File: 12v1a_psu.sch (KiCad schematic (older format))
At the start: 18 parts, among them J1 AC_in, J2 P1, J3 P2, J4 Vout, Q1 BD440, SW1 SW_SPST, U1 LM7812

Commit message: Work on pcb layout
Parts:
- J1, J2, J3, SW1: footprint Connector_Wire:SolderWirePad_1x02_P7.62mm_Drill2.5mm -> Connector_Wire:SolderWirePad_1x02_P5.08mm_Drill1.5mm
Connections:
- wire segments 65 -> 69
- no-connect marks 4 -> 0
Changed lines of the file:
@@
 F 0 "SW1" H 2150 3235 50  0000 C CNN
 F 1 "SW_SPST" H 2150 3144 50  0000 C CNN
-F 2 "Connector_Wire:SolderWirePad_1x02_P7.62mm_Drill2.5mm" H 2150 3000 50  0001 C CNN
+F 2 "Connector_Wire:SolderWirePad_1x02_P5.08mm_Drill1.5mm" H 2150 3000 50  0001 C CNN
 F 3 "~" H 2150 3000 50  0001 C CNN
 	1    2150 3000
@@
 Wire Wire Line
 	2450 3000 2450 2750
-NoConn ~ 3500 2950
-NoConn ~ 3500 3050
 Wire Wire Line
 	6000 3000 6650 3000
@@
 F 0 "J1" H 1518 2775 50  0000 C CNN
 F 1 "AC_in" H 1518 2866 50  0000 C CNN
-F 2 "Connector_Wire:SolderWirePad_1x02_P7.62mm_Drill2.5mm" H 1600 3100 50  0001 C CNN
+F 2 "Connector_Wire:SolderWirePad_1x02_P5.08mm_Drill1.5mm" H 1600 3100 50  0001 C CNN
 F 3 "~" H 1600 3100 50  0001 C CNN
 	1    1600 3100
@@
 F 0 "J2" V 2814 2262 50  0000 R CNN
 F 1 "P1" V 2723 2262 50  0000 R CNN
-F 2 "Connector_Wire:SolderWirePad_1x02_P7.62mm_Drill2.5mm" H 2850 2450 50  0001 C CNN
+F 2 "Connector_Wire:SolderWirePad_1x02_P5.08mm_Drill1.5mm" H 2850 2450 50  0001 C CNN
 F 3 "~" H 2850 2450 50  0001 C CNN
 	1    2850 2450
@@
 F 0 "J3" V 2822 3630 50  0000 L CNN
 F 1 "P2" V 2913 3630 50  0000 L CNN
-F 2 "Connector_Wire:SolderWirePad_1x02_P7.62mm_Drill2.5mm" H 2950 3550 50  0001 C CNN
+F 2 "Connector_Wire:SolderWirePad_1x02_P5.08mm_Drill1.5mm" H 2950 3550 50  0001 C CNN
 F 3 "~" H 2950 3550 50  0001 C CNN
 	1    2950 3550
 	0    1    1    0
 $EndComp
-NoConn ~ 2950 2650
 Wire Wire Line
 	2450 2750 2850 2750
@@
 	2850 2650 2850 2750
 Connection ~ 2850 2750
-NoConn ~ 2950 3350
 Wire Wire Line
 	2850 3350 2850 3250
@@
 Wire Wire Line
 	2450 3250 2850 3250
+Wire Wire Line
+	2950 3350 2950 3050
+Wire Wire Line
+	2950 3050 3500 3050
+Wire Wire Line
+	2950 2950 2950 2650
+Wire Wire Line
+	3500 2950 2950 2950
 $EndSCHEMATC

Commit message: Add filter caps, misc changes
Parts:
- removed J1: AC_in, Connector_Wire:SolderWirePad_1x02_P5.08mm_Drill1.5mm, symbol Connector_Generic:Conn_01x02
- removed Q1: BD440, Package_TO_SOT_THT:TO-126-3_Vertical, symbol Transistor_BJT:BD440
- removed SW1: SW_SPST, Connector_Wire:SolderWirePad_1x02_P5.08mm_Drill1.5mm, symbol Switch:SW_SPST
- removed U1: LM7812, Package_TO_SOT_THT:TO-220-3_Vertical, symbol Regulator_Linear:LM7812_TO220
- added C?: 1uF, symbol Device:C
- added C?: 2200u, Capacitor_THT:CP_Radial_D30.0mm_P10.00mm_SnapIn, symbol Device:CP
- added J?: AC_IN, symbol Connector_Generic:Conn_01x03
- added Q?: Q_PNP_BCE, symbol Device:Q_PNP_BCE
- added U1: L7812, Package_TO_SOT_THT:TO-220-3_Vertical, symbol Regulator_Linear:L7812
- C1: value 10000u -> 2200u
- R2: Field4 (none) -> 1/2W
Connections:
- net labels added: AC_E, AC_L, AC_N
- wire segments 69 -> 75
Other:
- note added: "TODO: use L01-6363 instead"
- moved on the sheet: C1, C2, C3, D5, J2, J3, J4, R1, TR1

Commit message: Clean up symbol/footprint libs, add cad models
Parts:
- removed J?: AC_IN, symbol Connector_Generic:Conn_01x03
- added H1, H2, H3, H4: PTH_M3, MountingHole:MountingHole_3.2mm_M3_Pad_Via, symbol Mechanical:MountingHole_Pad
- added J1: AC_IN, Connector_Wire:SolderWirePad_1x02_P5.08mm_Drill1.5mm, symbol Connector_Generic:Conn_01x02
- C1: footprint Capacitor_THT:CP_Radial_D30.0mm_P10.00mm_SnapIn -> (none)
- C2: renamed from C?; footprint Capacitor_THT:CP_Radial_D30.0mm_P10.00mm_SnapIn -> (none)
- C3: renamed from C?; footprint (none) -> Capacitor_THT:C_Rect_L18.0mm_W8.0mm_P15.00mm_FKS3_FKP3
- C4: renamed from C2; footprint Capacitor_THT:C_Disc_D5.0mm_W2.5mm_P2.50mm -> (none)
- C5: renamed from C3; footprint Capacitor_THT:C_Disc_D3.8mm_W2.6mm_P2.50mm -> (none)
- J4: footprint Connector_BarrelJack:BarrelJack_Horizontal -> 12v1a_psu:BarrelJack_Horizontal
- TR1: footprint L01-6353:Transformer_L01-6353 -> 12v1a_psu:L01-6363
- gave numbers to parts that had none: 1
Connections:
- net AC_L: now also J1.2 (Pin_2)
- net AC_N: now also J1.1 (Pin_1)
- net GND: now also H1.1, H2.1, H3.1, H4.1
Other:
- note removed: "TODO: use L01-6363 instead"
- moved on the sheet: C1, C2, C3, C4, C5, D1, D2, D3, D4, D5, J2, J3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

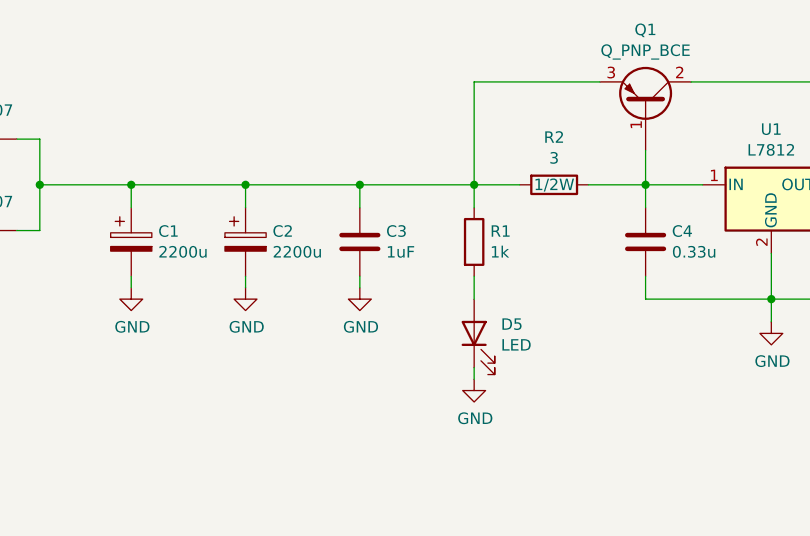
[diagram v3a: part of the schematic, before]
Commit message: Fix cap value
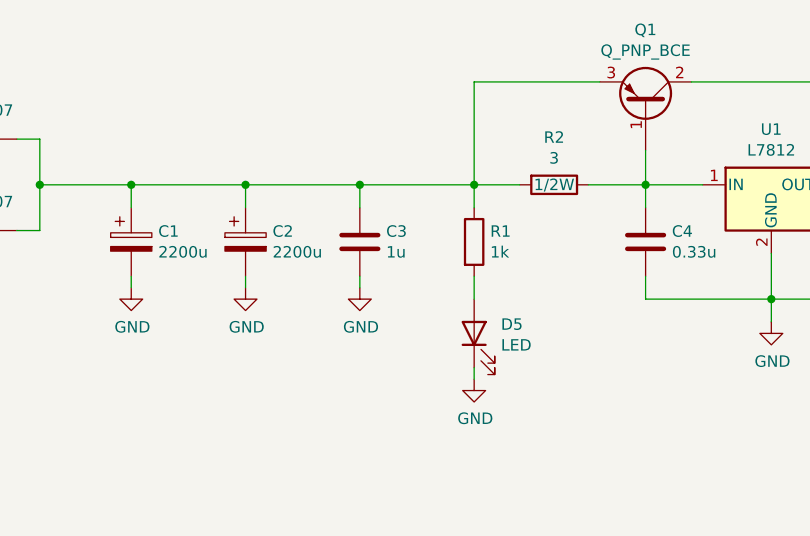
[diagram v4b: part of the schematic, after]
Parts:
- C3: value 1uF -> 1u
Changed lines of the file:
@@
 P 5850 3250
 F 0 "C3" H 5965 3296 50  0000 L CNN
-F 1 "1uF" H 5965 3205 50  0000 L CNN
+F 1 "1u" H 5965 3205 50  0000 L CNN
 F 2 "Capacitor_THT:C_Rect_L18.0mm_W8.0mm_P15.00mm_FKS3_FKP3" H 5888 3100 50  0001 C CNN
 F 3 "~" H 5850 3250 50  0001 C CNN

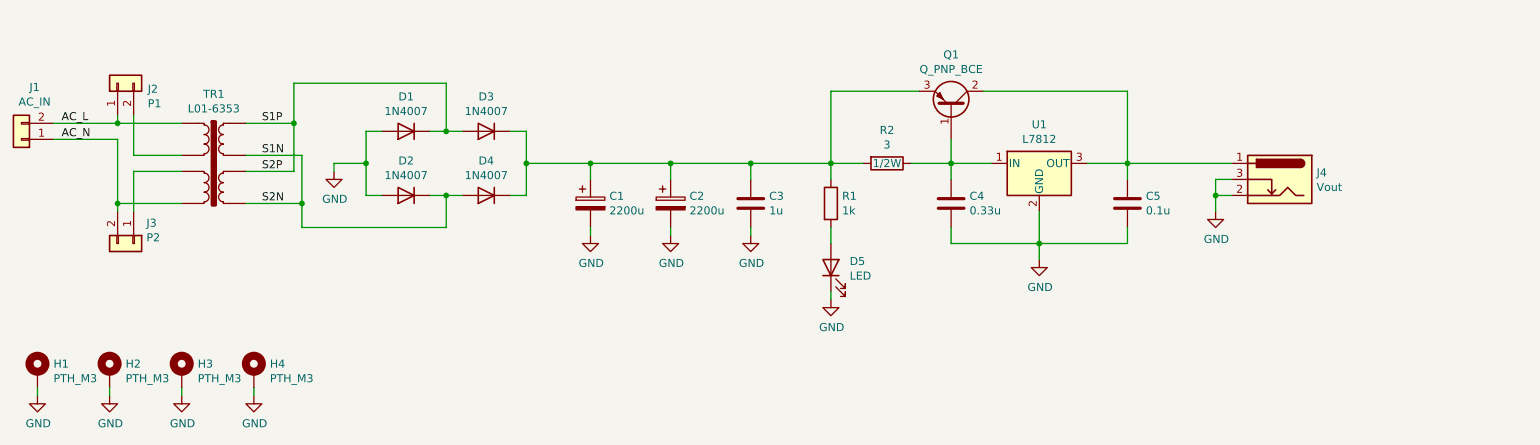
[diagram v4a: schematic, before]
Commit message: Chose bjt for reg, picked footprints
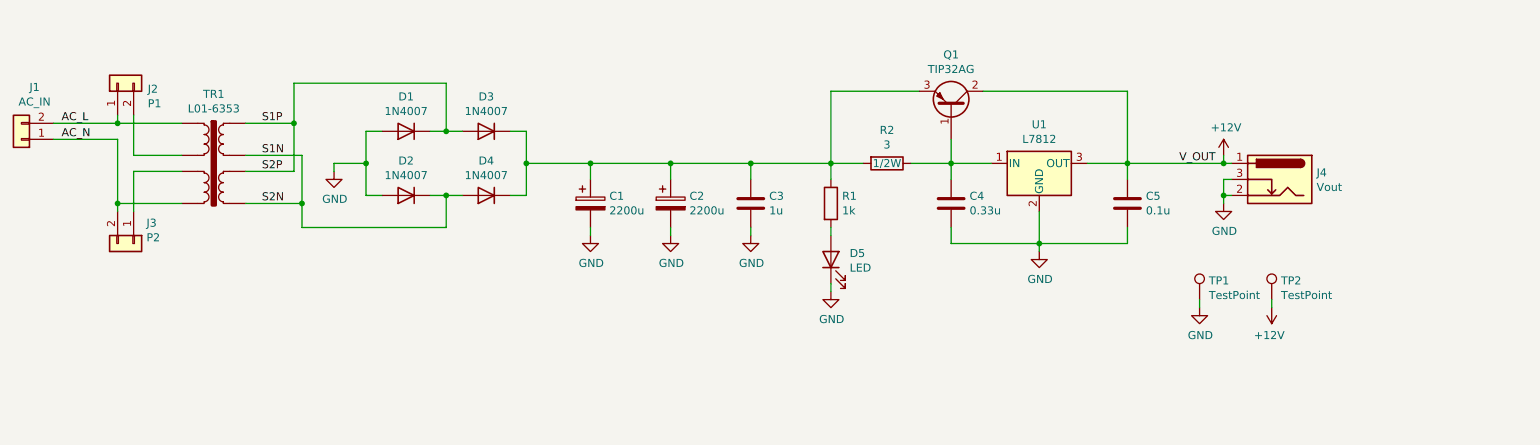
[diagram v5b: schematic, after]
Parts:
- removed H1, H2, H3, H4: PTH_M3, MountingHole:MountingHole_3.2mm_M3_Pad_Via, symbol Mechanical:MountingHole_Pad
- added TP1: TestPoint, TestPoint:TestPoint_THTPad_2.0x2.0mm_Drill1.0mm, symbol Connector:TestPoint
- added TP2: TestPoint, TestPoint:TestPoint_THTPad_D2.0mm_Drill1.0mm, symbol Connector:TestPoint
- C1, C2: footprint (none) -> Capacitor_THT:CP_Radial_D16.0mm_P7.50mm
- C4: footprint (none) -> Capacitor_THT:C_Rect_L7.2mm_W3.5mm_P5.00mm_FKS2_FKP2_MKS2_MKP2
- C5: footprint (none) -> Capacitor_THT:C_Rect_L7.2mm_W2.5mm_P5.00mm_FKS2_FKP2_MKS2_MKP2
- J1, J2, J3: footprint Connector_Wire:SolderWirePad_1x02_P5.08mm_Drill1.5mm -> Connector_Wire:SolderWire-0.75sqmm_1x02_P4.8mm_D1.25mm_OD2.3mm
- Q1: value Q_PNP_BCE -> TIP32AG; footprint (none) -> Package_TO_SOT_THT:TO-220-3_Vertical
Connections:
- net GND: now also TP1.1
- net +12V: now reaches C5.1, J4.1, Q1.2 (C), U1.3 (OUT)
- net +12V: now also TP2.1
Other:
- moved on the sheet: D5
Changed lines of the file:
@@
 F 0 "C1" H 4968 3296 50  0000 L CNN
 F 1 "2200u" H 4968 3205 50  0000 L CNN
-F 2 "" H 4888 3100 50  0001 C CNN
+F 2 "Capacitor_THT:CP_Radial_D16.0mm_P7.50mm" H 4888 3100 50  0001 C CNN
 F 3 "~" H 4850 3250 50  0001 C CNN
 	1    4850 3250
@@
 L Device:LED D5
 U 1 1 5CCC0EA2
-P 6350 3650
-F 0 "D5" V 6389 3533 50  0000 R CNN
-F 1 "LED" V 6298 3533 50  0000 R CNN
-F 2 "LED_THT:LED_D5.0mm_Horizontal_O1.27mm_Z3.0mm" H 6350 3650 50  0001 C CNN
-F 3 "~" H 6350 3650 50  0001 C CNN
-	1    6350 3650
+P 6350 3600
+F 0 "D5" V 6389 3483 50  0000 R CNN
+F 1 "LED" V 6298 3483 50  0000 R CNN
+F 2 "LED_THT:LED_D5.0mm_Horizontal_O1.27mm_Z3.0mm" H 6350 3600 50  0001 C CNN
+F 3 "~" H 6350 3600 50  0001 C CNN
+	1    6350 3600
 	0    -1   -1   0
 $EndComp
 Wire Wire Line
-	6350 3500 6350 3400
+	6350 3450 6350 3400
 $Comp
 L Device:R R1
@@
 $EndComp
 Wire Wire Line
-	6350 3850 6350 3800
+	6350 3800 6350 3750
 $Comp
 L power:GND #PWR09
 U 1 1 5CCC34E6
-P 6350 3850
-F 0 "#PWR09" H 6350 3600 50  0001 C CNN
-F 1 "GND" H 6355 3677 50  0000 C CNN
-F 2 "" H 6350 3850 50  0001 C CNN
-F 3 "" H 6350 3850 50  0001 C CNN
-	1    6350 3850
+P 6350 3800
+F 0 "#PWR09" H 6350 3550 50  0001 C CNN
+F 1 "GND" H 6355 3627 50  0000 C CNN
+F 2 "" H 6350 3800 50  0001 C CNN
+F 3 "" H 6350 3800 50  0001 C CNN
+	1    6350 3800
 	1    0    0    -1
 $EndComp
@@
 P 7100 2650
 F 0 "Q1" V 7428 2650 50  0000 C CNN
-F 1 "Q_PNP_BCE" V 7337 2650 50  0000 C CNN
-F 2 "" H 7300 2750 50  0001 C CNN
+F 1 "TIP32AG" V 7337 2650 50  0000 C CNN
+F 2 "Package_TO_SOT_THT:TO-220-3_Vertical" H 7300 2750 50  0001 C CNN
 F 3 "~" H 7100 2650 50  0001 C CNN
 	1    7100 2650
@@
 $EndComp
 Wire Wire Line
-	8200 3000 8850 3000
-Wire Wire Line
-	8750 3200 8750 3300
-Connection ~ 8750 3200
-Wire Wire Line
-	8850 3200 8750 3200
-Wire Wire Line
-	8750 3100 8750 3200
-Wire Wire Line
-	8850 3100 8750 3100
-Wire Wire Line
 	6350 2550 6900 2550
 Wire Wire Line
@@
 L power:GND #PWR011
 U 1 1 5CCF183A
-P 8750 3300
-F 0 "#PWR011" H 8750 3050 50  0001 C CNN
-F 1 "GND" H 8755 3127 50  0000 C CNN
-F 2 "" H 8750 3300 50  0001 C CNN
-F 3 "" H 8750 3300 50  0001 C CNN
-	1    8750 3300
+P 8800 3250
+F 0 "#PWR011" H 8800 3000 50  0001 C CNN
+F 1 "GND" H 8805 3077 50  0000 C CNN
+F 2 "" H 8800 3250 50  0001 C CNN
+F 3 "" H 8800 3250 50  0001 C CNN
+	1    8800 3250
 	1    0    0    -1
 $EndComp
@@
 Connection ~ 7650 3500
 Wire Wire Line
-	7650 3500 7650 3600
+	7650 3500 7650 3550
 Wire Wire Line
 	8200 3500 8200 3400
@@
 L power:GND #PWR010
 U 1 1 5CC06751
-P 7650 3600
-F 0 "#PWR010" H 7650 3350 50  0001 C CNN
-F 1 "GND" H 7655 3427 50  0000 C CNN
-F 2 "" H 7650 3600 50  0001 C CNN
-F 3 "" H 7650 3600 50  0001 C CNN
-	1    7650 3600
+P 7650 3550
+F 0 "#PWR010" H 7650 3300 50  0001 C CNN
+F 1 "GND" H 7655 3377 50  0000 C CNN
+F 2 "" H 7650 3550 50  0001 C CNN
+F 3 "" H 7650 3550 50  0001 C CNN
+	1    7650 3550
 	1    0    0    -1
 $EndComp
@@
 F 0 "C4" H 7215 3296 50  0000 L CNN
 F 1 "0.33u" H 7215 3205 50  0000 L CNN
-F 2 "" H 7138 3100 50  0001 C CNN
+F 2 "Capacitor_THT:C_Rect_L7.2mm_W3.5mm_P5.00mm_FKS2_FKP2_MKS2_MKP2" H 7138 3100 50  0001 C CNN
 F 3 "~" H 7100 3250 50  0001 C CNN
 	1    7100 3250
@@
 F 0 "C5" H 8315 3296 50  0000 L CNN
 F 1 "0.1u" H 8315 3205 50  0000 L CNN
-F 2 "" H 8238 3100 50  0001 C CNN
+F 2 "Capacitor_THT:C_Rect_L7.2mm_W2.5mm_P5.00mm_FKS2_FKP2_MKS2_MKP2" H 8238 3100 50  0001 C CNN
 F 3 "~" H 8200 3250 50  0001 C CNN
 	1    8200 3250
@@
 F 0 "C2" H 5468 3296 50  0000 L CNN
 F 1 "2200u" H 5468 3205 50  0000 L CNN
-F 2 "" H 5388 3100 50  0001 C CNN
+F 2 "Capacitor_THT:CP_Radial_D16.0mm_P7.50mm" H 5388 3100 50  0001 C CNN
 F 3 "~" H 5350 3250 50  0001 C CNN
 	1    5350 3250
@@
 Wire Wire Line
 	5350 3000 5850 3000
-$Comp
-L Mechanical:MountingHole_Pad H1
-U 1 1 5FB1F325
-P 1400 4300
-F 0 "H1" H 1500 4349 50  0000 L CNN
-F 1 "PTH_M3" H 1500 4258 50  0000 L CNN
-F 2 "MountingHole:MountingHole_3.2mm_M3_Pad_Via" H 1400 4300 50  0001 C CNN
-F 3 "~" H 1400 4300 50  0001 C CNN
-	1    1400 4300
-	1    0    0    -1
-$EndComp
-$Comp
-L power:GND #PWR01
-U 1 1 5FB21FB5
-P 1400 4450
-F 0 "#PWR01" H 1400 4200 50  0001 C CNN
-F 1 "GND" H 1405 4277 50  0000 C CNN
-F 2 "" H 1400 4450 50  0001 C CNN
-F 3 "" H 1400 4450 50  0001 C CNN
-	1    1400 4450
-	1    0    0    -1
-$EndComp
-Wire Wire Line
-	1400 4450 1400 4400
-$Comp
-L Mechanical:MountingHole_Pad H2
-U 1 1 5FB2637E
-P 1850 4300
-F 0 "H2" H 1950 4349 50  0000 L CNN
-F 1 "PTH_M3" H 1950 4258 50  0000 L CNN
-F 2 "MountingHole:MountingHole_3.2mm_M3_Pad_Via" H 1850 4300 50  0001 C CNN
-F 3 "~" H 1850 4300 50  0001 C CNN
-	1    1850 4300
-	1    0    0    -1
-$EndComp
-$Comp
-L power:GND #PWR02
-U 1 1 5FB26384
-P 1850 4450
-F 0 "#PWR02" H 1850 4200 50  0001 C CNN
-F 1 "GND" H 1855 4277 50  0000 C CNN
-F 2 "" H 1850 4450 50  0001 C CNN
-F 3 "" H 1850 4450 50  0001 C CNN
-	1    1850 4450
-	1    0    0    -1
-$EndComp
-Wire Wire Line
-	1850 4450 1850 4400
-$Comp
-L Mechanical:MountingHole_Pad H3
-U 1 1 5FB27F25
-P 2300 4300
-F 0 "H3" H 2400 4349 50  0000 L CNN
-F 1 "PTH_M3" H 2400 4258 50  0000 L CNN
-F 2 "MountingHole:MountingHole_3.2mm_M3_Pad_Via" H 2300 4300 50  0001 C CNN
-F 3 "~" H 2300 4300 50  0001 C CNN
-	1    2300 4300
-	1    0    0    -1
-$EndComp
-$Comp
-L power:GND #PWR03
-U 1 1 5FB27F2B
-P 2300 4450
-F 0 "#PWR03" H 2300 4200 50  0001 C CNN
-F 1 "GND" H 2305 4277 50  0000 C CNN
-F 2 "" H 2300 4450 50  0001 C CNN
-F 3 "" H 2300 4450 50  0001 C CNN
-	1    2300 4450
-	1    0    0    -1
-$EndComp
-Wire Wire Line
-	2300 4450 2300 4400
-$Comp
-L Mechanical:MountingHole_Pad H4
-U 1 1 5FB29C79
-P 2750 4300
-F 0 "H4" H 2850 4349 50  0000 L CNN
-F 1 "PTH_M3" H 2850 4258 50  0000 L CNN
-F 2 "MountingHole:MountingHole_3.2mm_M3_Pad_Via" H 2750 4300 50  0001 C CNN
-F 3 "~" H 2750 4300 50  0001 C CNN
-	1    2750 4300
-	1    0    0    -1
-$EndComp
-$Comp
-L power:GND #PWR04
-U 1 1 5FB29C7F
-P 2750 4450
-F 0 "#PWR04" H 2750 4200 50  0001 C CNN
-F 1 "GND" H 2755 4277 50  0000 C CNN
-F 2 "" H 2750 4450 50  0001 C CNN
-F 3 "" H 2750 4450 50  0001 C CNN
-	1    2750 4450
-	1    0    0    -1
-$EndComp
-Wire Wire Line
-	2750 4450 2750 4400
 Wire Wire Line
 	1900 2850 1900 3250
@@
 F 0 "J3" V 1872 3580 50  0000 L CNN
 F 1 "P2" V 1963 3580 50  0000 L CNN
-F 2 "Connector_Wire:SolderWirePad_1x02_P5.08mm_Drill1.5mm" H 2000 3500 50  0001 C CNN
+F 2 "Connector_Wire:SolderWire-0.75sqmm_1x02_P4.8mm_D1.25mm_OD2.3mm" H 2000 3500 50  0001 C CNN
 F 3 "~" H 2000 3500 50  0001 C CNN
 	1    2000 3500
@@
 F 0 "J2" V 1864 2312 50  0000 R CNN
 F 1 "P1" V 1773 2312 50  0000 R CNN
-F 2 "Connector_Wire:SolderWirePad_1x02_P5.08mm_Drill1.5mm" H 1900 2500 50  0001 C CNN
+F 2 "Connector_Wire:SolderWire-0.75sqmm_1x02_P4.8mm_D1.25mm_OD2.3mm" H 1900 2500 50  0001 C CNN
 F 3 "~" H 1900 2500 50  0001 C CNN
 	1    1900 2500
@@
 F 0 "J1" H 1218 2525 50  0000 C CNN
 F 1 "AC_IN" H 1218 2616 50  0000 C CNN
-F 2 "Connector_Wire:SolderWirePad_1x02_P5.08mm_Drill1.5mm" H 1300 2850 50  0001 C CNN
+F 2 "Connector_Wire:SolderWire-0.75sqmm_1x02_P4.8mm_D1.25mm_OD2.3mm" H 1300 2850 50  0001 C CNN
 F 3 "~" H 1300 2850 50  0001 C CNN
 	1    1300 2850
@@
 Text Label 1550 2750 0    50   ~ 0
 AC_L
+Text Label 8750 3000 2    50   ~ 0
+V_OUT
+$Comp
+L Connector:TestPoint TP1
+U 1 1 5FB2F260
+P 8650 3850
+F 0 "TP1" H 8708 3968 50  0000 L CNN
+F 1 "TestPoint" H 8708 3877 50  0000 L CNN
+F 2 "TestPoint:TestPoint_THTPad_2.0x2.0mm_Drill1.0mm" H 8850 3850 50  0001 C CNN
+F 3 "~" H 8850 3850 50  0001 C CNN
+	1    8650 3850
+	1    0    0    -1
+$EndComp
+$Comp
+L power:GND #PWR012
+U 1 1 5FB2FD10
+P 8650 3900
+F 0 "#PWR012" H 8650 3650 50  0001 C CNN
+F 1 "GND" H 8655 3727 50  0000 C CNN
+F 2 "" H 8650 3900 50  0001 C CNN
+F 3 "" H 8650 3900 50  0001 C CNN
+	1    8650 3900
+	1    0    0    -1
+$EndComp
+Wire Wire Line
+	8650 3900 8650 3850
+$Comp
+L Connector:TestPoint TP2
+U 1 1 5FB324EE
+P 9100 3850
+F 0 "TP2" H 9158 3968 50  0000 L CNN
+F 1 "TestPoint" H 9158 3877 50  0000 L CNN
+F 2 "TestPoint:TestPoint_THTPad_D2.0mm_Drill1.0mm" H 9300 3850 50  0001 C CNN
+F 3 "~" H 9300 3850 50  0001 C CNN
+	1    9100 3850
+	1    0    0    -1
+$EndComp
+$Comp
+L power:+12V #PWR014
+U 1 1 5FB32C70
+P 8800 2950
+F 0 "#PWR014" H 8800 2800 50  0001 C CNN
+F 1 "+12V" H 8815 3123 50  0000 C CNN
+F 2 "" H 8800 2950 50  0001 C CNN
+F 3 "" H 8800 2950 50  0001 C CNN
+	1    8800 2950
+	1    0    0    -1
+$EndComp
+Wire Wire Line
+	8850 3100 8800 3100
+Wire Wire Line
+	8800 3100 8800 3200
+Wire Wire Line
+	8850 3200 8800 3200
+Connection ~ 8800 3200
+Wire Wire Line
+	8800 3200 8800 3250
+Wire Wire Line
+	8800 3000 8800 2950
+Connection ~ 8800 3000
+Wire Wire Line
+	8800 3000 8850 3000
+Wire Wire Line
+	8200 3000 8800 3000
+$Comp
+L power:+12V #PWR013
+U 1 1 5FB3F00F
+P 9100 3900
+F 0 "#PWR013" H 9100 3750 50  0001 C CNN
+F 1 "+12V" H 9115 4073 50  0000 C CNN
+F 2 "" H 9100 3900 50  0001 C CNN
+F 3 "" H 9100 3900 50  0001 C CNN
+	1    9100 3900
+	-1   0    0    1
+$EndComp
+Wire Wire Line
+	9100 3900 9100 3850
 $EndSCHEMATC

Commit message: Add parts list, add case and ac receptable step files
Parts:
- J4: value Vout -> Barrel_Jack
- R2: Field4 1/2W -> 1W
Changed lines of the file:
@@
 F 2 "Resistor_THT:R_Axial_DIN0207_L6.3mm_D2.5mm_P10.16mm_Horizontal" V 6630 3000 50  0001 C CNN
 F 3 "~" H 6700 3000 50  0001 C CNN
-F 4 "1/2W" V 6700 3000 50  0000 C CNN "Field4"
+F 4 "1W" V 6700 3000 50  0000 C CNN "Field4"
 	1    6700 3000
 	0    1    1    0
@@
 P 9150 3100
 F 0 "J4" H 8920 3142 50  0000 R CNN
-F 1 "Vout" H 8920 3051 50  0000 R CNN
+F 1 "Barrel_Jack" H 8920 3051 50  0000 R CNN
 F 2 "12v1a_psu:BarrelJack_Horizontal" H 9200 3060 50  0001 C CNN
 F 3 "~" H 9200 3060 50  0001 C CNN
